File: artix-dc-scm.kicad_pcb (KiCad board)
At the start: 8 copper layers, 90 x 120.4 mm, 474 parts, among them IC1 TPS54561, IC2 TLV73312PDBVT, J1 L834-1G1T-S7, J12 S2B-PH-K-S_LF__SN_, J13 62000311121, J2 1-2199230-6, J3 543630489, J4 M20-7830642, J5 SFF-TA-1002-4C+, J6 0878311420, J7 61300611121, Q1 IRLML6402TRPBF, Q10 2N7002, Q11 2N7002, Q12 2N7002, Q13 2N7002, Q14 2N7002, Q15 2N7002, Q16 2N7002, Q2 IRLML6402TRPBF, Q3 IRLML6402TRPBF, Q4 IRLML6402TRPBF, Q5 IRLML6402TRPBF, Q6 IRLML6402TRPBF, Q7 2N7002, Q8 2N7002, Q9 2N7002, U1 MTFC16GAPALNA-AIT, U10 TPS62823DLCT, U11 TPS62823DLCT, U12 TPS62823DLCT, U13 TPS62823DLCT, U14 XC7A100T-FGG484, U15 SN74LVC1G08DCKR, U16 SN74LS08DBR, U17 USB3300-EZK-TR, U18 USB3300-EZK-TR, U2 W25Q32JVSSIQ_TR, U20 KSZ9031RNXCA, U3 W25Q32JVSSIQ_TR, U4 W25Q32JVSSIQ_TR, U5 W25Q32JVSSIQ_TR, U6 NVT2008DQ,115, U7 AS4C256M16D3, U8 TPS51200DRC, U9 LM3881MME_NOPB, Y1 TSX-3225, Y2 ABM8G-25.000MHZ-18-D2Y-T, Y3 TSX-3225

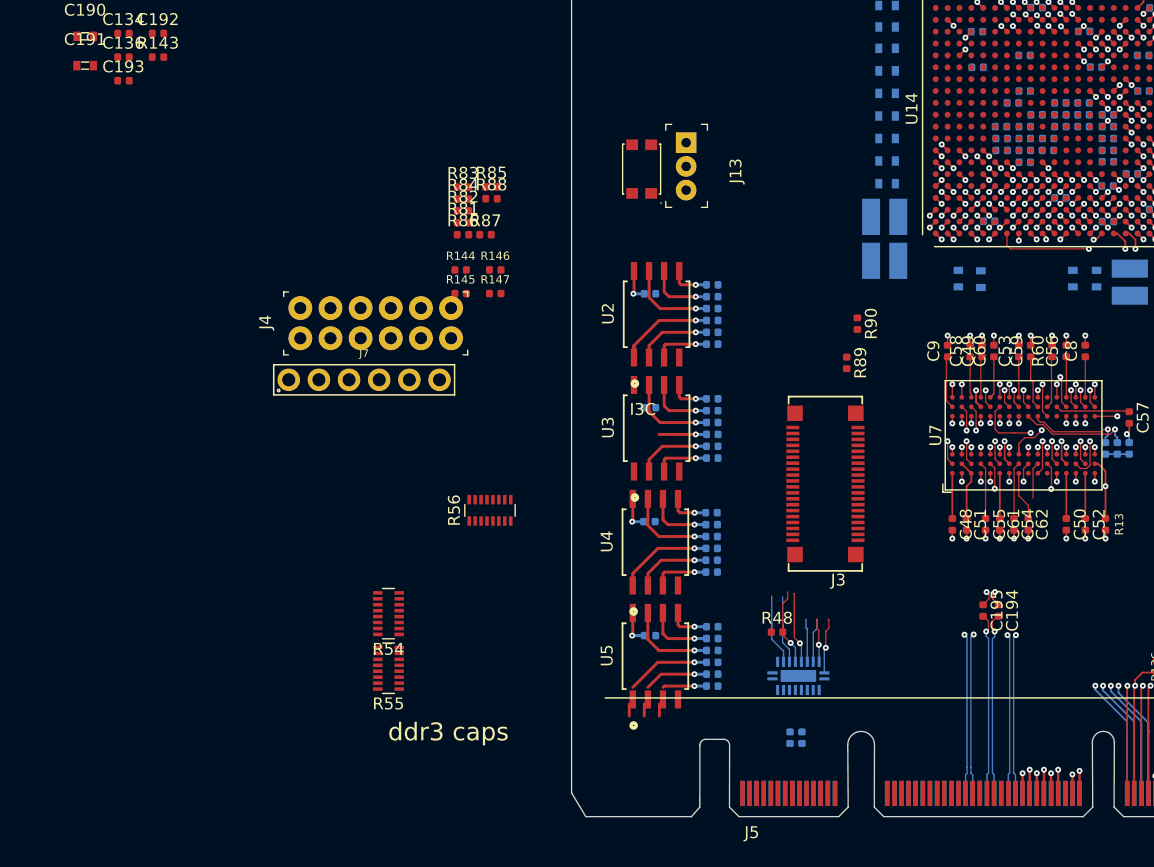
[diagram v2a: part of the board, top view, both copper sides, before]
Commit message: Break route low I2C
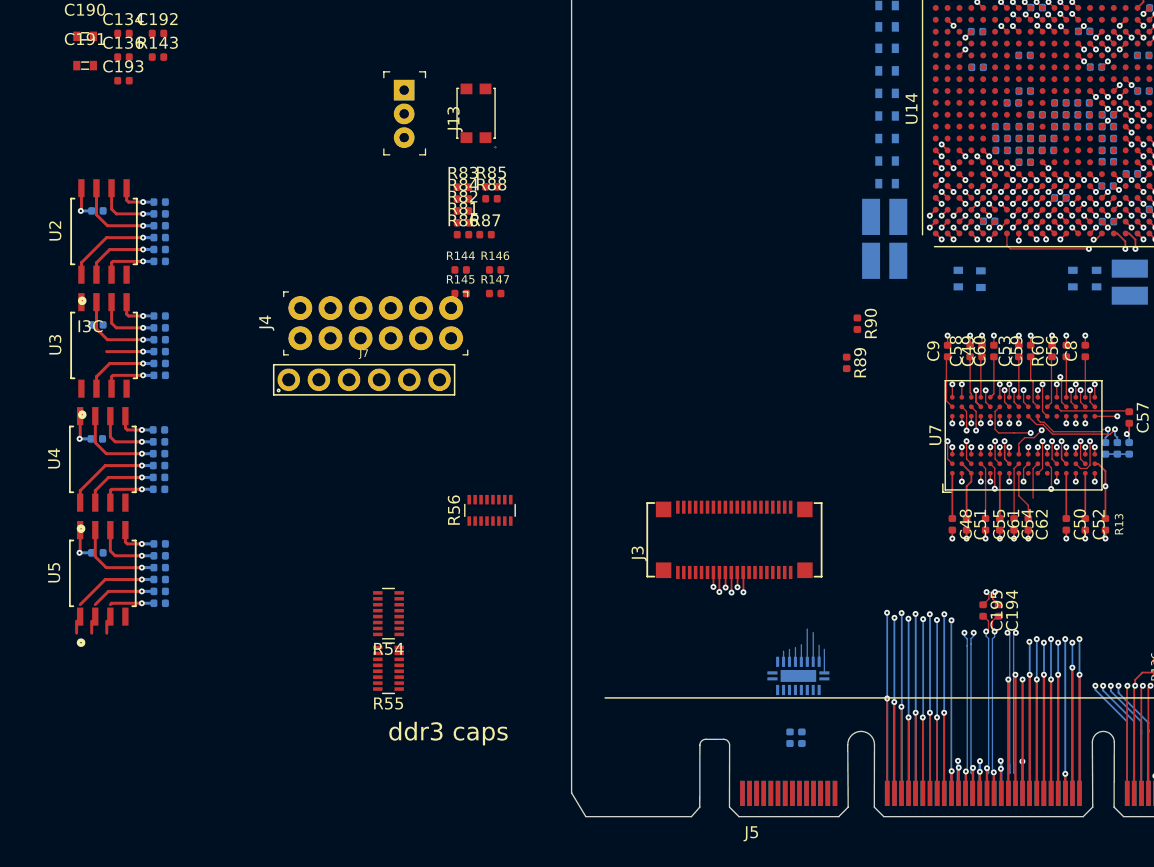
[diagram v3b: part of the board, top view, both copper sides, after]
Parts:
- removed R48: R_357k_0402, artix-dc-scm-footprints:0402-res
- moved C35 47.1 mm to (20.1, 128.3)
- moved C36 47.1 mm to (20.1, 137.9)
- moved C37 47.1 mm to (20.1, 147.5)
- moved C38 47.1 mm to (20.1, 157.1)
- moved R21 47.1 mm to (25.4, 130.5)
- moved R22 47.1 mm to (25.4, 140.1)
- moved R23 47.1 mm to (25.4, 149.7)
- moved R24 47.1 mm to (25.4, 159.3)
- moved R25 47.1 mm to (25.4, 128.5)
- moved R26 47.1 mm to (25.4, 138.1)
- moved R27 47.1 mm to (25.4, 147.7)
- moved R28 47.1 mm to (25.4, 157.3)
- moved R29 47.1 mm to (25.4, 127.5)
- moved R30 47.1 mm to (25.4, 137.1)
- moved R31 47.1 mm to (25.3, 146.7)
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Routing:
- net I2C[8]_SDA: track 0.00 -> 69.9 mm, vias 0 -> 1
- net I2C[8]_SCL: track 0.00 -> 68.4 mm, vias 0 -> 1
- net I2C[7]_SDA: track 0.00 -> 67.8 mm, vias 0 -> 1
- net I2C[7]_SCL: track 0.00 -> 66.1 mm, vias 0 -> 1
- net NCSI_RXD1: track 1.90 -> 67.8 mm
- net I2C[6]_SDA: track 0.00 -> 65.8 mm, vias 0 -> 1
- net I2C[6]_SCL: track 0.00 -> 64.4 mm, vias 0 -> 1
- net NCSI_RXD0: track 1.60 -> 65.8 mm
- net I2C[5]_SDA: track 0.00 -> 64.1 mm, vias 0 -> 1
- net NCSI_RXER: track 1.90 -> 65.9 mm
- net NCSI_TXD1: track 1.60 -> 63.9 mm
- net I2C[5]_SCL: track 0.00 -> 62.0 mm, vias 0 -> 1
- net NCSI_TXD0: track 1.90 -> 63.6 mm
- net NCSI_CRS_DV: track 0.00 -> 61.5 mm, vias 0 -> 1
- net NCSI_TXEN: track 1.60 -> 61.7 mm
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
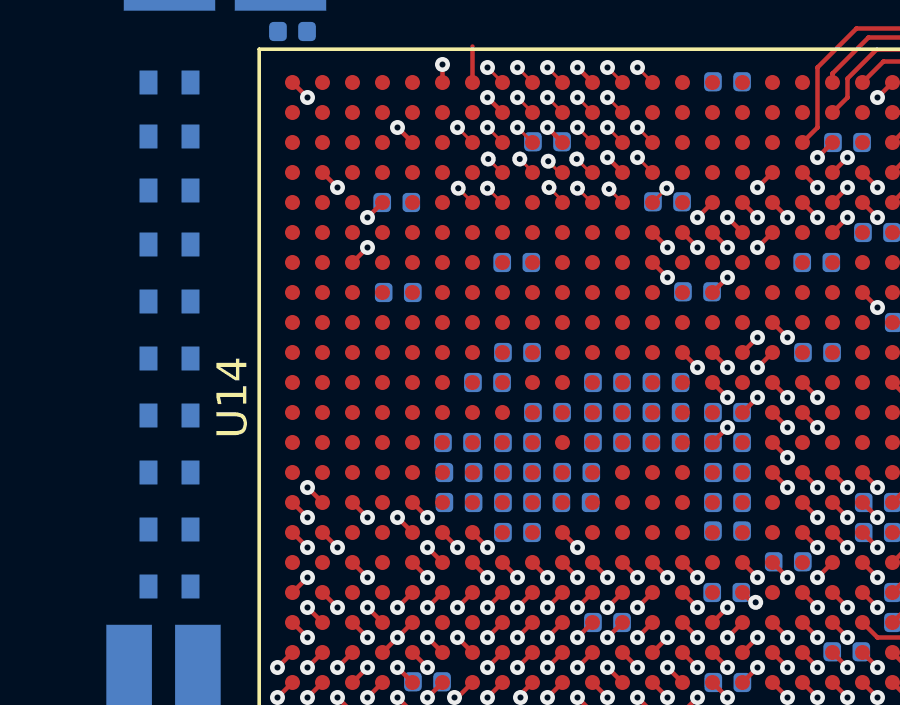
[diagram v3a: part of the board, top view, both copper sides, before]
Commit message: Route low speed IO towards FPGA
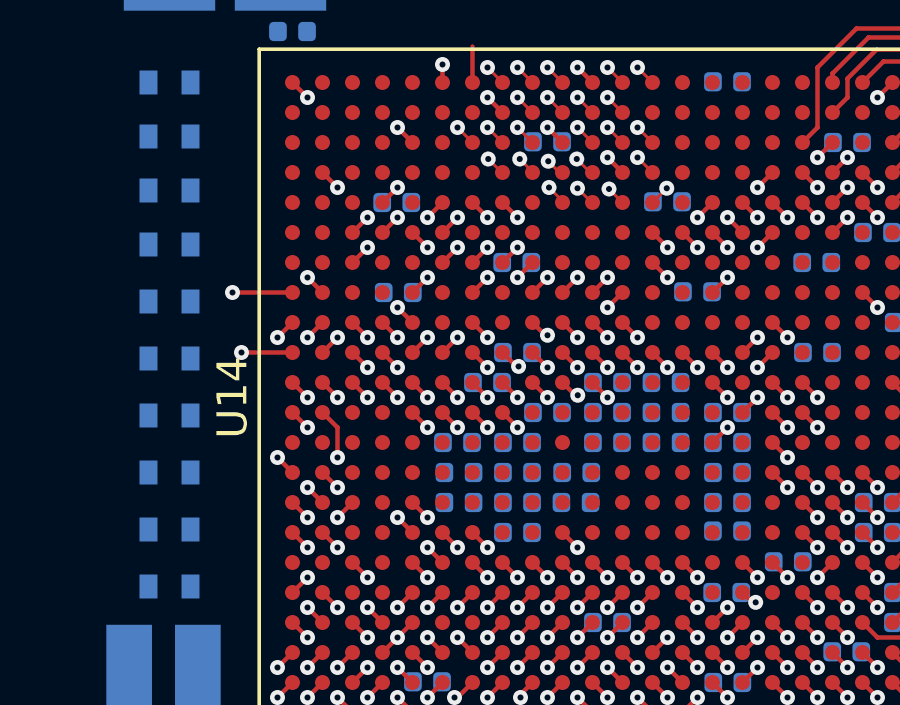
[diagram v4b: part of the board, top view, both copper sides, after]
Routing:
- net I2C[1]_SCL: track 51.4 -> 74.7 mm, vias 1 -> 2
- net I2C[1]_SDA: track 51.4 -> 73.8 mm, vias 1 -> 2
- net I2C[0]_SDA: track 50.6 -> 72.8 mm, vias 1 -> 2
- net I2C[0]_SCL: track 50.2 -> 71.8 mm, vias 1 -> 2
- net I2C[2]_SCL: track 52.4 -> 73.8 mm, vias 1 -> 2
- net ESPI_IO3: track 52.7 -> 73.7 mm
- net ESPI_IO2: track 52.2 -> 72.9 mm
- net ESPI_CS1_N: track 52.5 -> 72.9 mm
- net ESPI_IO0: track 52.9 -> 72.8 mm
- net ESPI_IO1: track 52.6 -> 72.5 mm
- net ESPI_CLK: track 57.7 -> 77.6 mm
- net I2C[3]_SDA: track 53.3 -> 72.9 mm, vias 1 -> 2
- net I2C[3]_SCL: track 52.7 -> 72.2 mm, vias 1 -> 2
- net ESPI_CS0_N: track 57.9 -> 76.5 mm
- net I2C[4]_SDA: track 54.5 -> 72.7 mm
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
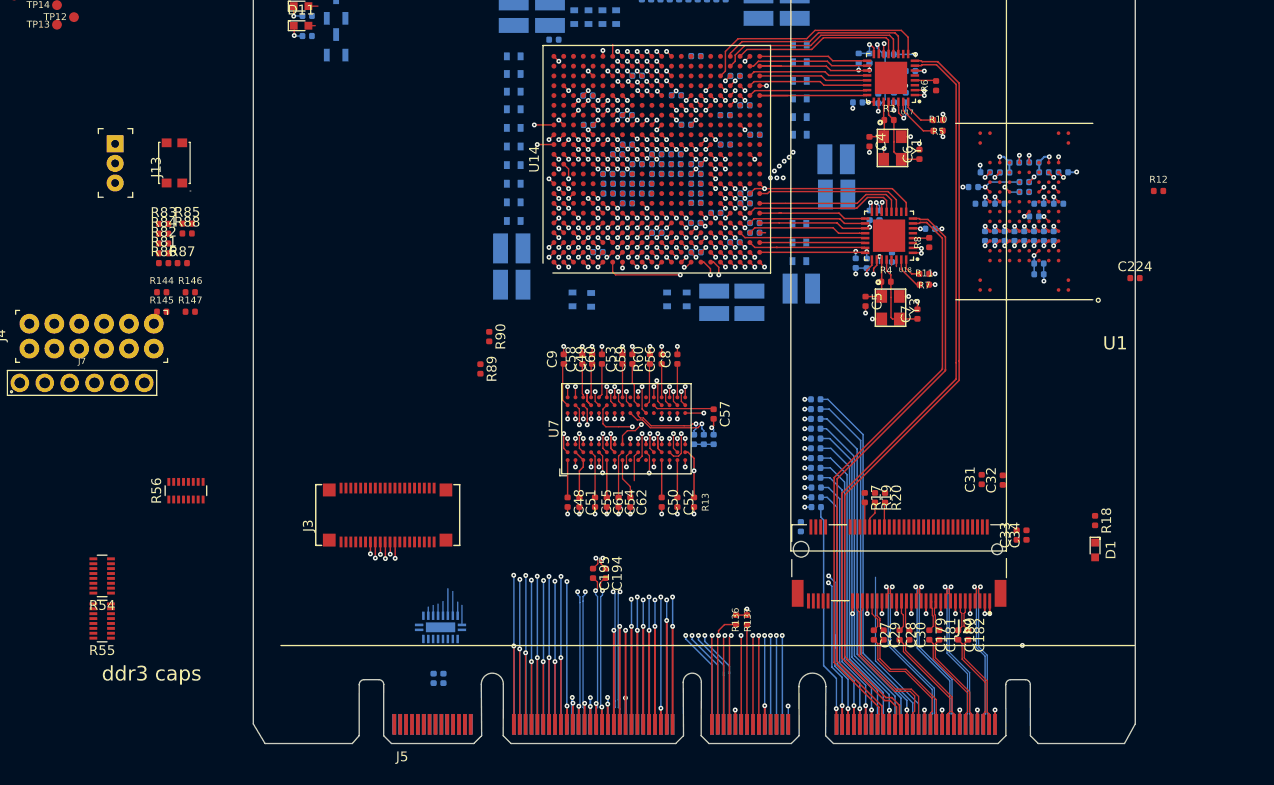
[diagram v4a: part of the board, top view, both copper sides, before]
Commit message: Connect low speed IOs to FPGA
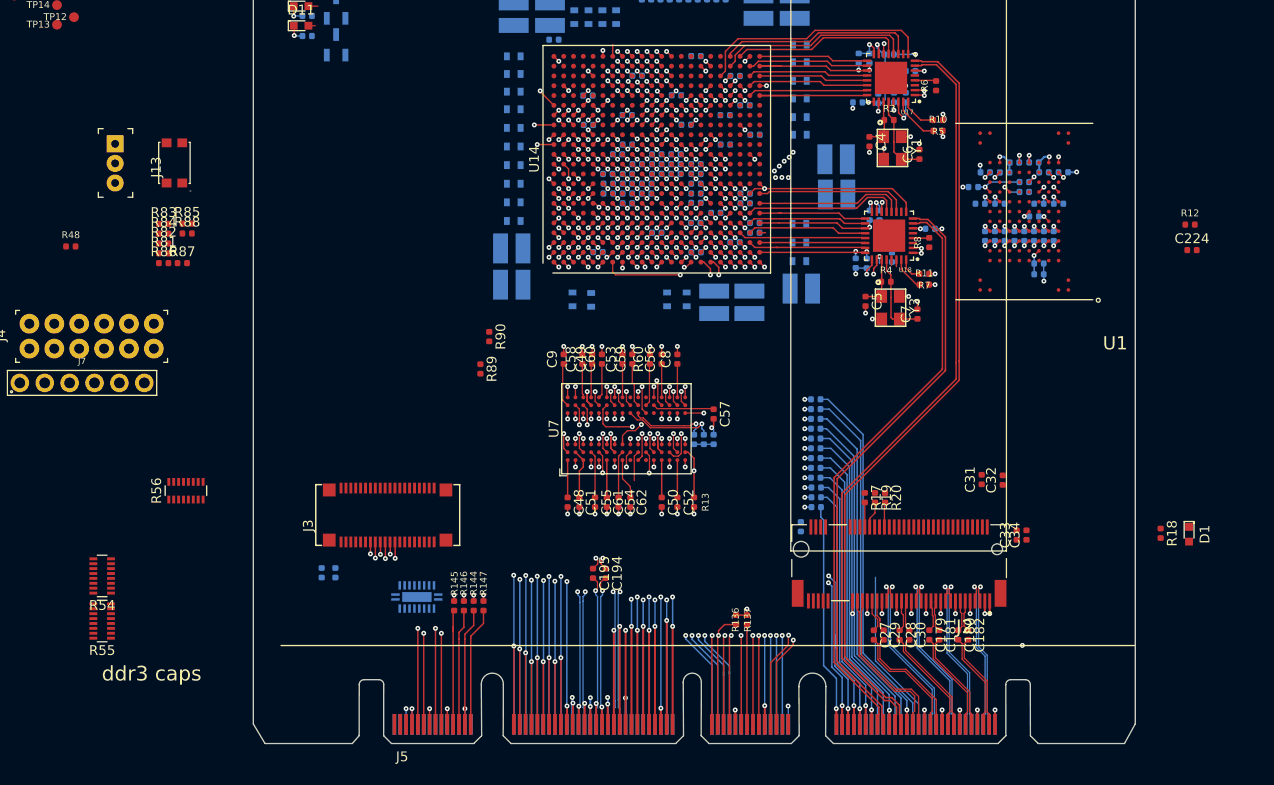
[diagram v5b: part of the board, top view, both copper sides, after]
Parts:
- added R48: R_357k_0402, artix-dc-scm-footprints:0402-res, F.Cu at (41.5, 128.6)
- moved R144 45.1 mm to (82.6, 165.2), turned to 270 degrees
- moved R146 42.5 mm to (81.6, 165.2), turned to 270 degrees
- moved R147 42.4 mm to (83.6, 165.2), turned to 270 degrees
- moved R145 42.3 mm to (80.6, 165.2), turned to 270 degrees
- moved R114 15.7 mm to (67.1, 161.9)
- moved R115 15.4 mm to (68.5, 161.9)
- moved D1 9.72 mm to (155.6, 157.9)
- moved R18 6.81 mm to (152.7, 157.8)
- moved C224 6.48 mm to (155.9, 128.9)
- moved R12 4.70 mm to (155.7, 126.3)
- moved U6 3.93 mm to (76.8, 164.3)
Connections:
- net EMCCLK renamed Net-(U14-PadV22)
- R144 pad 1: Net-(R144-Pad1) -> SPIO_MOSI_R
- R145 pad 1: Net-(R145-Pad1) -> SPIO_CLK_R
- R146 pad 1: Net-(R146-Pad1) -> SPIO_CS_N_R
- R147 pad 1: Net-(R147-Pad1) -> SPIO_MISO_R
- U14 pad A13: Net-(U14-PadA13) -> NCSI_TXEN
- U14 pad A14: Net-(U14-PadA14) -> NCSI_CRS_DV
- U14 pad A15: Net-(U14-PadA15) -> NCSI_RXD0
- U14 pad A16: Net-(U14-PadA16) -> SPIO_MOSI_R
- U14 pad B13: Net-(U14-PadB13) -> NCSI_CLK
- U14 pad B15: Net-(U14-PadB15) -> NCSI_RXD1
- U14 pad B16: Net-(U14-PadB16) -> SPIO_MISO_R
- U14 pad C13: Net-(U14-PadC13) -> I2C[8]_SCL
- U14 pad C14: Net-(U14-PadC14) -> I2C[8]_SDA
- U14 pad C15: Net-(U14-PadC15) -> NCSI_RXER
- U14 pad D14: Net-(U14-PadD14) -> NCSI_TXD0
- U14 pad D16: Net-(U14-PadD16) -> SPIO_CS_N_R
- U14 pad D17: Net-(U14-PadD17) -> UART0_SCM_RX
- U14 pad E13: Net-(U14-PadE13) -> I2C[7]_SDA
- U14 pad E14: Net-(U14-PadE14) -> NCSI_TXD1
- U14 pad E16: Net-(U14-PadE16) -> SPIO_CLK_R
- U14 pad E17: Net-(U14-PadE17) -> UART0_SCM_TX
- U14 pad F13: Net-(U14-PadF13) -> I2C[7]_SCL
- U14 pad G13: I2C[1]_SDA -> I2C[6]_SDA
- U14 pad G15: Net-(U14-PadG15) -> ESPI_CS1_N
- U14 pad G18: SGPIO_INTR_N -> Net-(U14-PadG18)
- U14 pad H13: I2C[0]_SCL -> I2C[6]_SCL
- U14 pad H14: I2C[2]_SDA -> Net-(U14-PadH14)
- U14 pad H18: SGPIO_RESET_N -> ESPI_ALERT_N
- U14 pad J14: I2C[2]_SCL -> I2C[2]_SDA
- U14 pad J15: Net-(U14-PadJ15) -> I2C[0]_SDA
- U14 pad J16: I2C[8]_SDA -> I2C[0]_SCL
- U14 pad J17: I2C[10]_SCL -> Net-(U14-PadJ17)
- U14 pad K13: Net-(U14-PadK13) -> I2C[4]_SCL
- U14 pad K16: I2C[8]_SCL -> ESPI_IO2
- U14 pad K17: I2C[9]_SCL -> ESPI_IO0
- U14 pad K18: Net-(U14-PadK18) -> ESPI_CS0_N
- U14 pad L13: I2C[0]_SDA -> I2C[4]_SDA
- U14 pad L14: I2C[3]_SDA -> I2C[2]_SCL
- U14 pad L15: I2C[7]_SDA -> I2C[1]_SCL
- U14 pad L16: I2C[7]_SCL -> ESPI_IO3
- U14 pad L18: Net-(U14-PadL18) -> ESPI_CLK
- U14 pad M13: I2C[1]_SCL -> I2C[3]_SDA
- U14 pad M15: I2C[5]_SDA -> I2C[1]_SDA
- U14 pad M16: I2C[6]_SDA -> ESPI_IO1
- U14 pad M17: I2C[6]_SCL -> ESPI_RESET_N
- U14 pad N13: Net-(U14-PadN13) -> I2C[5]_SCL
- U14 pad N14: Net-(U14-PadN14) -> I2C[5]_SDA
- U14 pad U5: Net-(U14-PadU5) -> SGPIO_RESET_N
- U14 pad U7: Net-(U14-PadU7) -> SGPIO_INTR_N
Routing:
- net UART1_SCM_TX: track 0.00 -> 88.4 mm, vias 0 -> 2
- net UART1_SCM_RX: track 0.00 -> 87.7 mm, vias 0 -> 2
- net UART0_SCM_TX: track 0.00 -> 77.7 mm, vias 0 -> 2
- net UART0_SCM_RX: track 0.00 -> 74.3 mm, vias 0 -> 2
- net SGPIO_RESET_N: track 0.73 -> 67.4 mm, vias 1 -> 2
- net SGPIO_INTR_N: track 0.71 -> 66.7 mm, vias 1 -> 2
- net SPIO_CLK_R: track 0.00 -> 61.6 mm, vias 0 -> 2
- net SPIO_CS_N_R: track 0.00 -> 60.7 mm, vias 0 -> 2
- net SPIO_MISO_R: track 0.00 -> 56.2 mm, vias 0 -> 2
- net SPIO_MOSI_R: track 0.00 -> 55.9 mm, vias 0 -> 2
- net GND: track 180.8 -> 210.2 mm, vias 168 -> 201
- net SPIO_MISO: track 0.00 -> 12.2 mm
- net SPIO_CLK: track 0.00 -> 12.1 mm
- net SPIO_MOSI: track 0.00 -> 12.0 mm
- net SPIO_CS_N: track 0.00 -> 11.8 mm
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
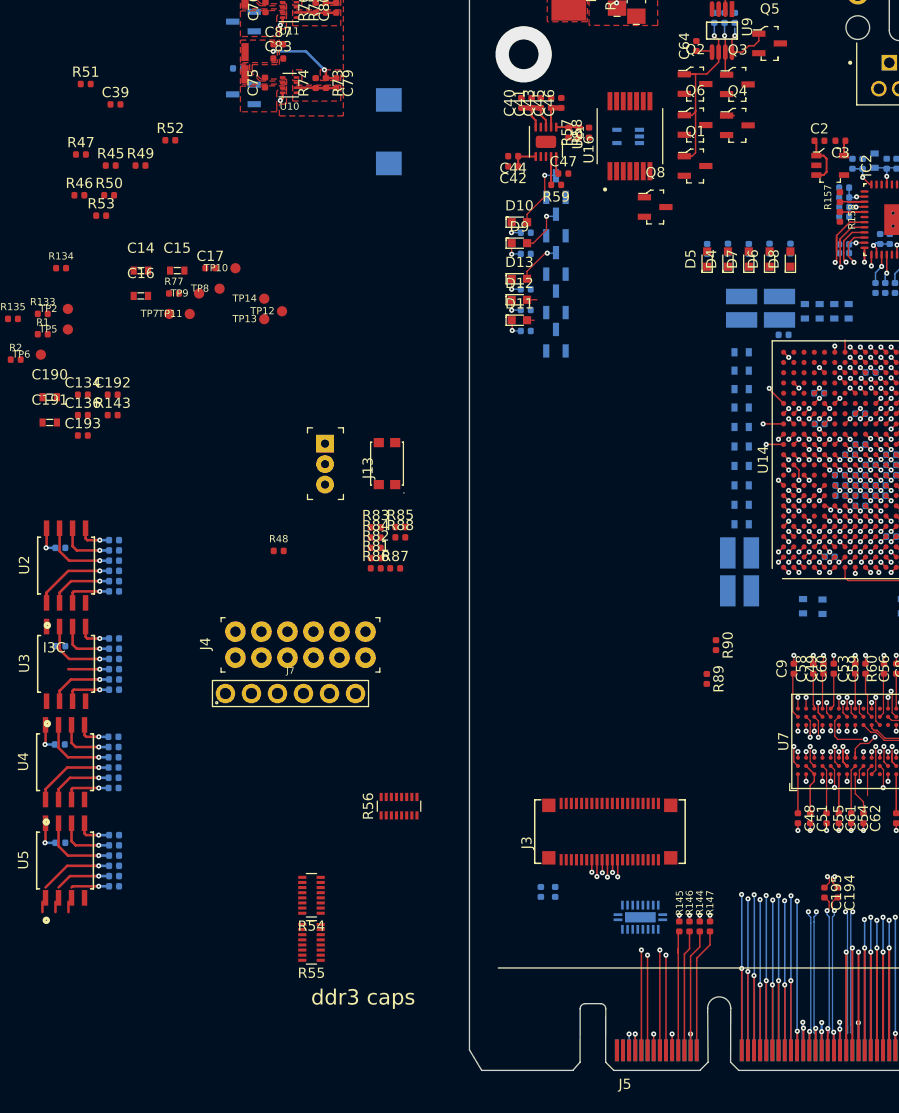
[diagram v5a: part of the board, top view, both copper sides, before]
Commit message: Routed I3C signals
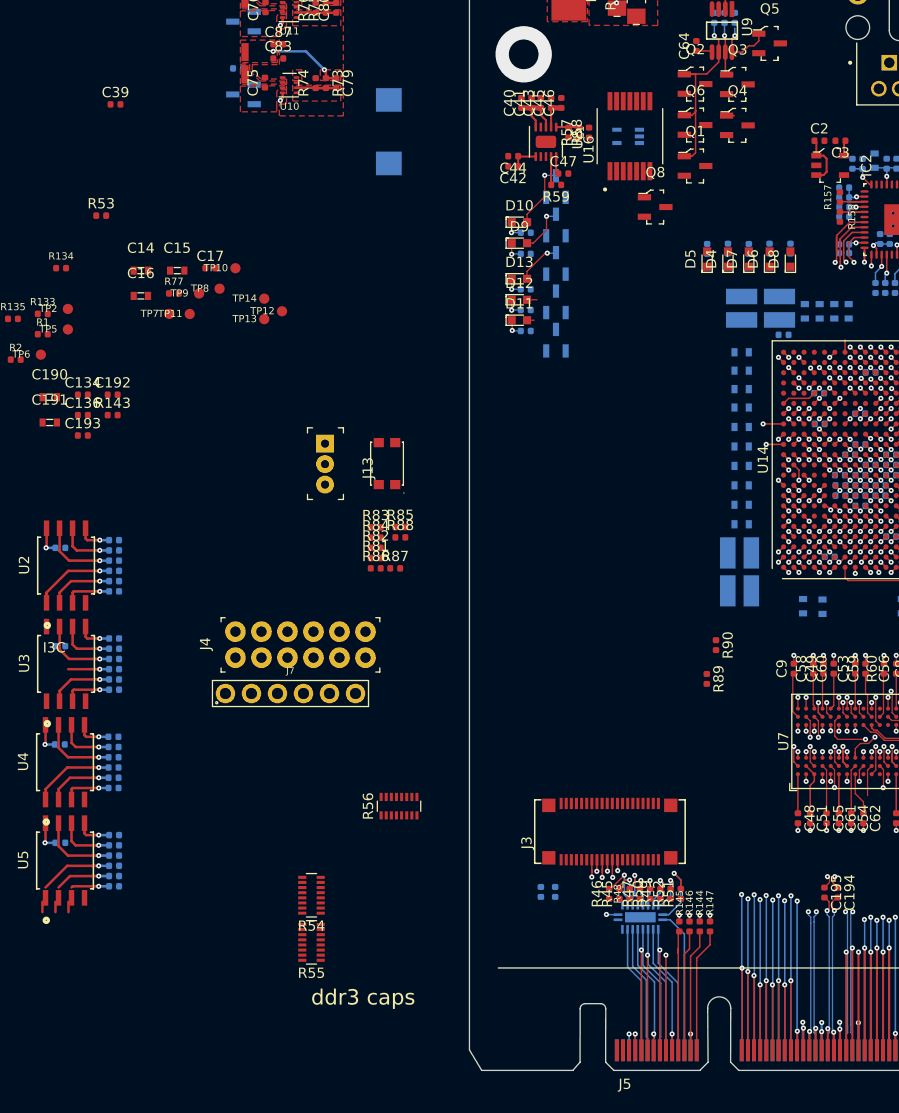
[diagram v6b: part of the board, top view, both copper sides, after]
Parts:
- moved R51 98.1 mm to (80.7, 162.1), turned to 90 degrees
- moved R47 90.5 mm to (76.7, 162.1), turned to 90 degrees
- moved R52 88.3 mm to (79.7, 162.1), turned to 90 degrees
- moved R49 87.4 mm to (78.7, 162.1), turned to 90 degrees
- moved R45 86.7 mm to (74.7, 162.1), turned to 90 degrees
- moved R50 86.3 mm to (77.7, 162.1), turned to 90 degrees
- moved R46 85.6 mm to (73.7, 162.1), turned to 90 degrees
- moved R48 47.9 mm to (75.7, 162.1), turned to 90 degrees
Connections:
- U14 pad A21: Net-(U14-PadA21) -> I3C[0]_SCL_3V3
- U14 pad B20: Net-(U14-PadB20) -> I3C[0]_SDA_3V3
- U14 pad C19: Net-(U14-PadC19) -> I3C[2]_SCL_3V3
- U14 pad D19: Net-(U14-PadD19) -> I3C[3]_SCL_3V3
- U14 pad D20: Net-(U14-PadD20) -> I3C[1]_SCL_3V3
- U14 pad F18: Net-(U14-PadF18) -> I3C[3]_SDA_3V3
- U14 pad F19: Net-(U14-PadF19) -> I3C[2]_SDA_3V3
- U14 pad F20: Net-(U14-PadF20) -> I3C[1]_SDA_3V3
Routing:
- net I3C[3]_SDA_3V3: track 0.00 -> 67.3 mm, vias 0 -> 2
- net I3C[1]_SDA_3V3: track 0.00 -> 66.7 mm, vias 0 -> 2
- net I3C[1]_SCL_3V3: track 0.00 -> 66.3 mm, vias 0 -> 2
- net I3C[0]_SCL_3V3: track 0.00 -> 66.1 mm, vias 0 -> 2
- net I3C[0]_SDA_3V3: track 0.00 -> 65.1 mm, vias 0 -> 2
- net I3C[2]_SDA_3V3: track 0.00 -> 64.9 mm, vias 0 -> 2
- net I3C[2]_SCL_3V3: track 0.00 -> 62.8 mm, vias 0 -> 2
- net I3C[3]_SCL_3V3: track 0.00 -> 62.1 mm, vias 0 -> 2
- net I3C[3]_SDA: track 0.00 -> 14.0 mm
- net I3C[3]_SCL: track 0.00 -> 12.6 mm
- net I3C[2]_SDA: track 0.00 -> 12.6 mm
- net I3C[1]_SDA: track 0.00 -> 12.6 mm
- net I3C[2]_SCL: track 0.00 -> 12.5 mm
- net I3C[1]_SCL: track 0.00 -> 12.5 mm
- net I3C[0]_SDA: track 0.00 -> 12.4 mm
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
